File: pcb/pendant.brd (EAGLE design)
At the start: 24 x 99 mm, 45 parts, among them CON1 USB_MICROSMT+THRUHULE, Q2 16MHz, SW2 BUTTON_2, T1 SSM3J328R,LF, T2 SSM3J328R,LF, U2 MK20D--VFM5, U3 74LVC1G17DCK, U4 74LVC1G17DCK

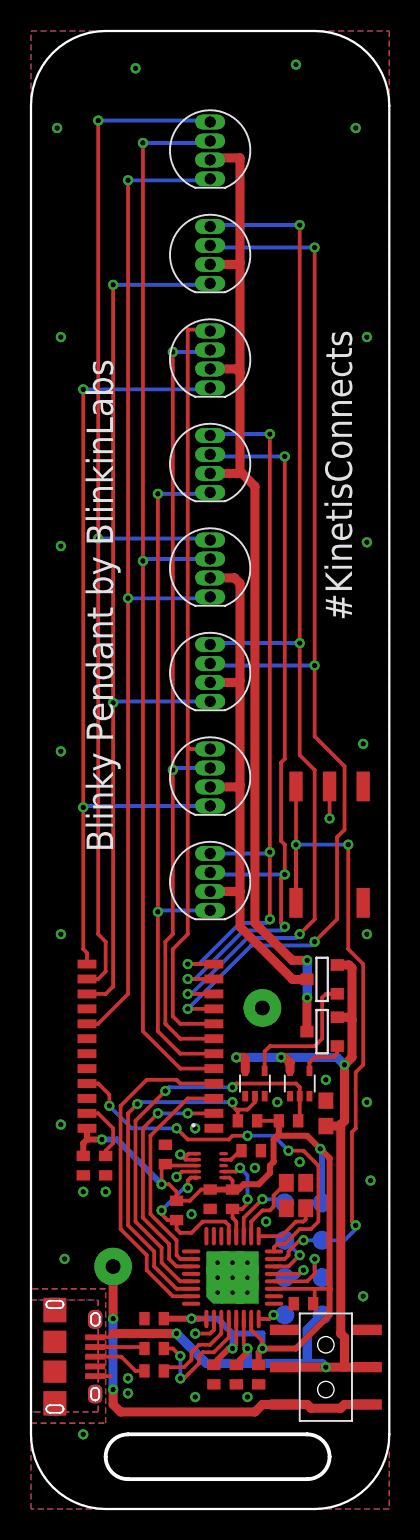
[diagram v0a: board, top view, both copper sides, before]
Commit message: fix cap under ICN2026, change led output order, use 5050 LEDs, replace power and tach switches, use 10 LEDs, move test points out from battery
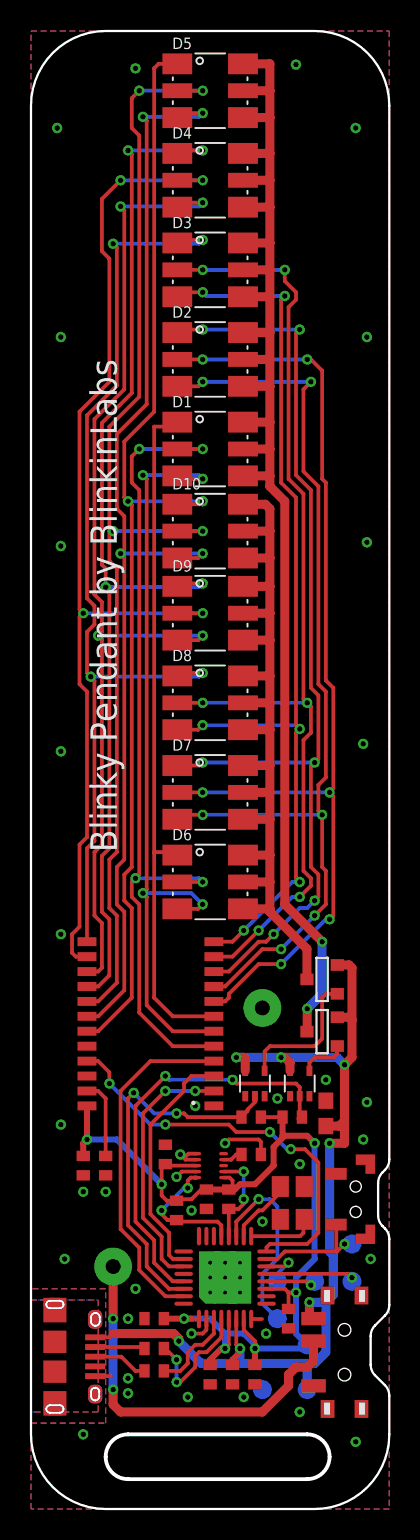
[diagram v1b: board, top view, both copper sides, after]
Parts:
- removed U$13: SWITCH_SPDTMSS-22C02, LeoBlinky2014:MSS-22C02
- added D10, D5: LED-RGB5050, blinkinlabs:LED-TRICOLOR-5050-FIXED
- added U$2: SWITCH_SPDT_SHIELD, blinkinlabs:SWITCH_SMD_90_DEGREE
- D1, D2, D3, D4, D6, D7, D8, D9: value LED-RGB-CA-THRUCLEAR -> LED-RGB5050; device SparkFun-LED:LED-RGB-THRU -> blinkinlabs:LED-TRICOLOR-5050-FIXED
- Q2: device blinkinlabs:CRSYTAL_2520 -> blinkinlabs:CRYSTAL_3225
- SW2: device blinkinlabs:TD-07XB -> blinkinlabs:BUTTON_MOMENTARY_MP5
- moved SW2 23.8 mm to (21.8, 20.8)
- moved TP2 9.55 mm to (18.5, 11.0)
- moved TP1 7.77 mm to (16.5, 12.8)
- moved TP5 5.22 mm to (15.5, 8.00)
- moved TP6 5.10 mm to (18.5, 8.00)
- moved TP7 4.51 mm to (21.5, 15.2)
- moved D9 3.00 mm to (12.0, 60.0), turned to 0 degrees
- moved TP4 2.80 mm to (16.5, 15.2)
- moved TP8 2.02 mm to (21.5, 17.8)
- moved D4 2.00 mm to (12.0, 89.0), turned to 0 degrees
- moved D8 2.00 mm to (12.0, 54.0), turned to 0 degrees
- moved U$5 1.50 mm to (8.00, 32.5)
- moved C15 1.41 mm to (17.2, 12.8), turned to 270 degrees
- moved D1 1.00 mm to (12.0, 71.0), turned to 0 degrees
- moved D3 1.00 mm to (12.0, 83.0), turned to 0 degrees
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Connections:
- removed net N$16: U$5.20
- net +5V: now also U$2.L1; no longer U$13.P0, U$13.P1
- net B0: now also D1.1, D6.1, U$5.7; no longer D1.4, D6.4, U$5.12
- net B1: now also D2.1, D7.1, U$5.10; no longer D2.4, D7.4, U$5.8
- net B2: now also D3.1, D8.1, U$5.13; no longer D3.4, D8.4, U$5.10
- net B3: now also D4.1, D9.1, U$5.16; no longer D4.4, D9.4, U$5.14
- net B4: now also D10.1, D5.1, U$5.19; no longer U$5.16
- net G0: now also U$5.6; no longer U$5.11
- net G1: now also U$5.9; no longer U$5.7
- net G2: now also U$5.12; no longer U$5.9
- net G3: now also U$5.15; no longer U$5.5
- net G4: now also D10.3, D5.3
- net GND: now also SW2.1, SW2.SHEILD_1, SW2.SHEILD_2, SW2.SHEILD_3, SW2.SHEILD_4, U$2.SHIELD_1, U$2.SHIELD_2, U$2.SHIELD_3, U$2.SHIELD_4; no longer SW2.3, SW2.4, SW2.5
- net N$2: now also U$2.COM; no longer U$13.O0, U$13.O1
- net R0: now also D1.2, D6.2, U$5.5; no longer D1.1, D6.1, U$5.6
- net R1: now also D2.2, D7.2, U$5.8; no longer D2.1, D7.1, U$5.13
- net R2: now also D3.2, D8.2, U$5.11; no longer D3.1, D8.1, U$5.15
- net R3: now also D4.2, D9.2, U$5.14; no longer D4.1, D9.1, U$5.17
- net R4: now also D10.2, D5.2, U$5.17; no longer U$5.19
- net S0: now also D1.4, D1.5, D1.6, D2.4, D2.5, D2.6, D3.4, D3.5, D3.6, D4.4, D4.5, D4.6, D5.4, D5.5, D5.6; no longer D1.2, D2.2, D3.2, D4.2
- net S1: now also D10.4, D10.5, D10.6, D6.4, D6.5, D6.6, D7.4, D7.5, D7.6, D8.4, D8.5, D8.6, D9.4, D9.5, D9.6; no longer D6.2, D7.2, D8.2, D9.2
- net TMS: no longer SW2.1
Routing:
- net R4: track 0.00 -> 78.0 mm, vias 0 -> 4
- net G4: track 0.00 -> 76.7 mm, vias 0 -> 4
- net B4: track 0.00 -> 76.1 mm, vias 0 -> 2
- net TMS: track 48.2 -> 7.81 mm, vias 4 -> 1
- net S0: track 69.4 -> 93.7 mm
- net S1: track 37.2 -> 59.7 mm
- net B1: track 52.5 -> 65.8 mm, vias 0 -> 6
- net R1: track 55.7 -> 67.8 mm, vias 2 -> 6
- net G2: track 74.4 -> 63.3 mm, vias 4 -> 6
- net G1: track 54.0 -> 64.9 mm, vias 2 -> 6
- net R0: track 47.5 -> 56.8 mm, vias 2 -> 4
- net RESET: track 4.60 -> 12.9 mm
- net B2: track 71.3 -> 65.8 mm
- net R2: track 62.0 -> 67.2 mm, vias 2 -> 6
- net +5V: track 70.8 -> 66.4 mm, vias 6 -> 7
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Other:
- outline, holes or cut-outs redrawn
- board text removed: "#KinetisConnects"
- board text removed: "+5"
- board text removed: "BLUE"
- board text removed: "GREEN"
- board text removed: "RED"

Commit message: Update battery footprint
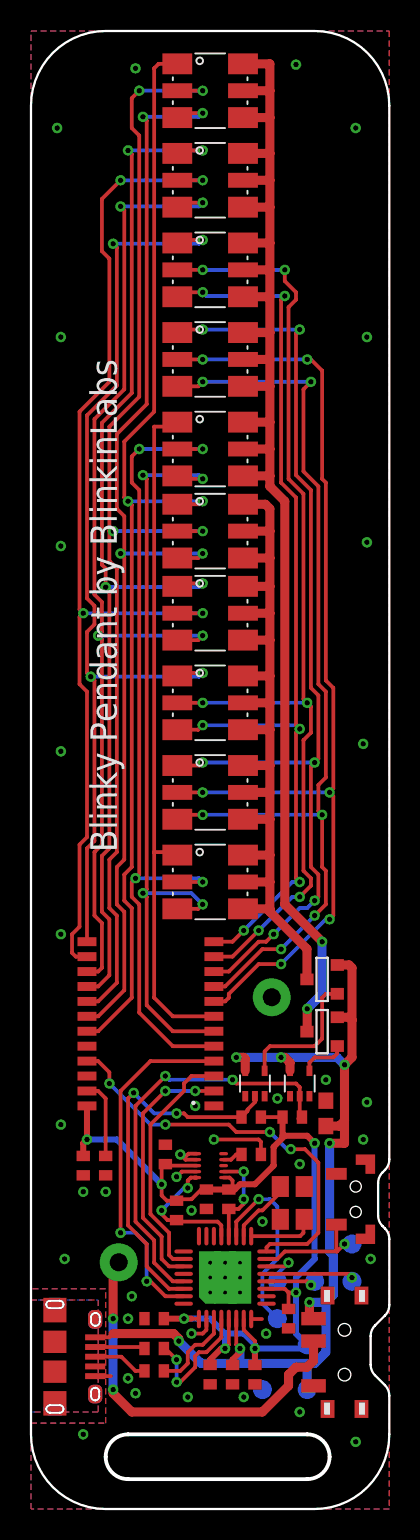
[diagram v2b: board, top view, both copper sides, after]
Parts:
- moved U$1 0.71 mm to (12.5, 28.0)
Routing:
- net LED_STROBE: track 23.3 -> 24.0 mm, vias 0 -> 2
- net GND: track 11.9 -> 12.6 mm
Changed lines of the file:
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@@
 <?xml version="1.0" encoding="utf-8"?>
 <!DOCTYPE eagle SYSTEM "eagle.dtd">
-<eagle version="7.1.0">
+<eagle version="7.2.0">
 <drawing>
 <settings>
@@
 <layer number="27" name="tValues" color="7" fill="1" visible="no" active="yes"/>
 <layer number="28" name="bValues" color="7" fill="1" visible="no" active="yes"/>
-<layer number="29" name="tStop" color="7" fill="3" visible="yes" active="yes"/>
+<layer number="29" name="tStop" color="7" fill="3" visible="no" active="yes"/>
 <layer number="30" name="bStop" color="7" fill="6" visible="no" active="yes"/>
-<layer number="31" name="tCream" color="13" fill="4" visible="yes" active="yes"/>
+<layer number="31" name="tCream" color="13" fill="4" visible="no" active="yes"/>
 <layer number="32" name="bCream" color="7" fill="5" visible="no" active="yes"/>
 <layer number="33" name="tFinish" color="6" fill="3" visible="no" active="yes"/>
 <layer number="34" name="bFinish" color="6" fill="6" visible="no" active="yes"/>
 <layer number="35" name="tGlue" color="7" fill="4" visible="no" active="yes"/>
-<layer number="36" name="bGlue" color="7" fill="5" visible="yes" active="yes"/>
+<layer number="36" name="bGlue" color="7" fill="5" visible="no" active="yes"/>
 <layer number="37" name="tTest" color="7" fill="1" visible="no" active="yes"/>
 <layer number="38" name="bTest" color="7" fill="1" visible="no" active="yes"/>
@@
 <element name="C3" library="adafruit" package="C0402" value="100nF" x="11.75" y="20.75" smashed="yes" rot="R270"/>
 <element name="C5" library="adafruit" package="C0402" value="100nF" x="9" y="23.75" smashed="yes" rot="R90"/>
-<element name="D1" library="blinkinlabs" package="LED-TRICOLOR-5050-FIXED" value="LED-RGB5050" x="12" y="71"/>
-<element name="D2" library="blinkinlabs" package="LED-TRICOLOR-5050-FIXED" value="LED-RGB5050" x="12" y="77"/>
-<element name="D3" library="blinkinlabs" package="LED-TRICOLOR-5050-FIXED" value="LED-RGB5050" x="12" y="83"/>
-<element name="D4" library="blinkinlabs" package="LED-TRICOLOR-5050-FIXED" value="LED-RGB5050" x="12" y="89"/>
-<element name="D6" library="blinkinlabs" package="LED-TRICOLOR-5050-FIXED" value="LED-RGB5050" x="12" y="42"/>
-<element name="D7" library="blinkinlabs" package="LED-TRICOLOR-5050-FIXED" value="LED-RGB5050" x="12" y="48"/>
-<element name="D8" library="blinkinlabs" package="LED-TRICOLOR-5050-FIXED" value="LED-RGB5050" x="12" y="54"/>
-<element name="D9" library="blinkinlabs" package="LED-TRICOLOR-5050-FIXED" value="LED-RGB5050" x="12" y="60"/>
+<element name="D1" library="blinkinlabs" package="LED-TRICOLOR-5050-FIXED" value="LED-RGB5050" x="12" y="71" smashed="yes">
+<attribute name="VALUE" x="9.46" y="67.444" size="0.762" layer="27"/>
+</element>
+<element name="D2" library="blinkinlabs" package="LED-TRICOLOR-5050-FIXED" value="LED-RGB5050" x="12" y="77" smashed="yes">
+<attribute name="VALUE" x="9.46" y="73.444" size="0.762" layer="27"/>
+</element>
+<element name="D3" library="blinkinlabs" package="LED-TRICOLOR-5050-FIXED" value="LED-RGB5050" x="12" y="83" smashed="yes">
+<attribute name="VALUE" x="9.46" y="79.444" size="0.762" layer="27"/>
+</element>
+<element name="D4" library="blinkinlabs" package="LED-TRICOLOR-5050-FIXED" value="LED-RGB5050" x="12" y="89" smashed="yes">
+<attribute name="VALUE" x="9.46" y="85.444" size="0.762" layer="27"/>
+</element>
+<element name="D6" library="blinkinlabs" package="LED-TRICOLOR-5050-FIXED" value="LED-RGB5050" x="12" y="42" smashed="yes">
+<attribute name="VALUE" x="9.46" y="38.444" size="0.762" layer="27"/>
+</element>
+<element name="D7" library="blinkinlabs" package="LED-TRICOLOR-5050-FIXED" value="LED-RGB5050" x="12" y="48" smashed="yes">
+<attribute name="VALUE" x="9.46" y="44.444" size="0.762" layer="27"/>
+</element>
+<element name="D8" library="blinkinlabs" package="LED-TRICOLOR-5050-FIXED" value="LED-RGB5050" x="12" y="54" smashed="yes">
+<attribute name="VALUE" x="9.46" y="50.444" size="0.762" layer="27"/>
+</element>
+<element name="D9" library="blinkinlabs" package="LED-TRICOLOR-5050-FIXED" value="LED-RGB5050" x="12" y="60" smashed="yes">
+<attribute name="VALUE" x="9.46" y="56.444" size="0.762" layer="27"/>
+</element>
 <element name="C11" library="adafruit" package="C0402" value="100nF" x="15" y="9" smashed="yes" rot="R270">
 <attribute name="VALUE" x="13.095" y="9.635" size="1.27" layer="27" rot="R270"/>
@@
 <attribute name="TP_SIGNAL_NAME" value="" x="16.5" y="12.75" size="1.778" layer="28" rot="MR0" display="off"/>
 </element>
-<element name="U$1" library="blinkinlabs" package="CR2032X2" value="CR2032X2" x="12" y="27.5" rot="MR300"/>
+<element name="U$1" library="blinkinlabs" package="CR2032X2" value="CR2032X2" x="12.5" y="28" rot="MR300"/>
 <element name="T1" library="zetex" package="SOT-23" value="SSM3J328R,LF" x="19.5" y="32" smashed="yes" rot="R270">
 <attribute name="OC_NEWARK" value="unknown" x="19.5" y="32" size="1.778" layer="27" rot="R270" display="off"/>
@@
 <attribute name="VALUE" x="16.575" y="23.585" size="1.27" layer="27" rot="R270"/>
 </element>
-<element name="D5" library="blinkinlabs" package="LED-TRICOLOR-5050-FIXED" value="LED-RGB5050" x="12" y="95"/>
-<element name="D10" library="blinkinlabs" package="LED-TRICOLOR-5050-FIXED" value="LED-RGB5050" x="12" y="65.5"/>
+<element name="D5" library="blinkinlabs" package="LED-TRICOLOR-5050-FIXED" value="LED-RGB5050" x="12" y="95" smashed="yes">
+<attribute name="VALUE" x="9.46" y="91.444" size="0.762" layer="27"/>
+</element>
+<element name="D10" library="blinkinlabs" package="LED-TRICOLOR-5050-FIXED" value="LED-RGB5050" x="12" y="65.5" smashed="yes">
+<attribute name="VALUE" x="9.46" y="61.944" size="0.762" layer="27"/>
+</element>
 <element name="U$2" library="blinkinlabs" package="SWITCH_SMD_90_DEGREE" value="SWITCH_SPDT_SHIELD" x="21" y="10.5" smashed="yes" rot="R270">
 <attribute name="VALUE" x="24" y="9.5" size="0.762" layer="27" rot="R270"/>
@@
 <via x="19.75" y="28.75" extent="1-16" drill="0.35"/>
 <via x="11" y="27" extent="1-16" drill="0.35"/>
-<via x="13" y="24.5" extent="1-16" drill="0.35"/>
+<via x="12.25" y="24.75" extent="1-16" drill="0.35"/>
 <wire x1="11.1" y1="22.6" x2="10.1" y2="22.6" width="0.254" layer="1"/>
 <wire x1="10.1" y1="22.6" x2="9.75" y2="22.25" width="0.254" layer="1"/>
@@
 <via x="22.5" y="27.25" extent="1-16" drill="0.35"/>
 <contactref element="U$1" pad="-"/>
-<via x="6.5" y="7.75" extent="1-16" drill="0.35"/>
+<via x="7" y="7.75" extent="1-16" drill="0.35"/>
 <via x="2.25" y="16.75" extent="1-16" drill="0.35"/>
 <via x="2" y="25.75" extent="1-16" drill="0.35"/>
@@
 <via x="18" y="6.5" extent="1-16" drill="0.35"/>
 <via x="21.75" y="4.5" extent="1-16" drill="0.35"/>
-<via x="7" y="14.75" extent="1-16" drill="0.35"/>
+<via x="6.75" y="14.25" extent="1-16" drill="0.35"/>
 <contactref element="SW2" pad="SHEILD_2"/>
 <contactref element="SW2" pad="SHEILD_3"/>
@@
 <wire x1="15.4" y1="23.75" x2="15.4" y2="24.6" width="0.254" layer="1"/>
 <wire x1="15.4" y1="24.6" x2="15.25" y2="24.75" width="0.254" layer="1"/>
-<wire x1="15.25" y1="24.75" x2="13.25" y2="24.75" width="0.254" layer="1"/>
-<wire x1="13.25" y1="24.75" x2="13" y2="24.5" width="0.254" layer="1"/>
+<wire x1="15.25" y1="24.75" x2="12.25" y2="24.75" width="0.254" layer="1"/>
 </signal>
 <signal name="LED_OE">
@@
 <wire x1="12.25" y1="30" x2="8" y2="30" width="0.254" layer="1"/>
 <wire x1="8" y1="30" x2="6" y2="28" width="0.254" layer="1"/>
-<wire x1="6" y1="28" x2="6" y2="18.75" width="0.254" layer="1"/>
+<wire x1="6" y1="28" x2="6" y2="18.5" width="0.254" layer="1"/>
 <wire x1="10.225" y1="14.25" x2="9" y2="14.25" width="0.254" layer="1"/>
-<wire x1="9" y1="14.25" x2="7.25" y2="16" width="0.254" layer="1"/>
-<wire x1="7.25" y1="16" x2="7.25" y2="17.5" width="0.254" layer="1"/>
-<wire x1="7.25" y1="17.5" x2="6" y2="18.75" width="0.254" layer="1"/>
+<via x="6" y="18.5" extent="1-16" drill="0.35"/>
+<wire x1="6" y1="18.5" x2="7" y2="18.5" width="0.254" layer="16"/>
+<wire x1="7" y1="18.5" x2="7.75" y2="17.75" width="0.254" layer="16"/>
+<wire x1="7.75" y1="17.75" x2="7.75" y2="15.25" width="0.254" layer="16"/>
+<via x="7.75" y="15.25" extent="1-16" drill="0.35"/>
+<wire x1="7.75" y1="15.25" x2="8" y2="15.25" width="0.254" layer="1"/>
+<wire x1="8" y1="15.25" x2="9" y2="14.25" width="0.254" layer="1"/>
 </signal>
 <signal name="LED_S0">
@@
 <signal name="N$2">
 <contactref element="U$1" pad="+"/>
-<wire x1="5.5" y1="16.24166875" x2="5.5" y2="12.75" width="0.6096" layer="1"/>
+<wire x1="5.875" y1="16.5251625" x2="5.5" y2="16.1501625" width="0.6096" layer="1"/>
+<wire x1="5.5" y1="16.1501625" x2="5.5" y2="12.75" width="0.6096" layer="1"/>
 <via x="5.5" y="12.75" extent="1-16" drill="0.35"/>
 <wire x1="5.5" y1="12.75" x2="5.5" y2="8" width="0.6096" layer="16"/>
 <via x="5.5" y="8" extent="1-16" drill="0.35"/>
-<wire x1="5.5" y1="8" x2="5.5" y2="7" width="0.6096" layer="1"/>
-<wire x1="5.5" y1="7" x2="6" y2="6.5" width="0.6096" layer="1"/>
-<wire x1="6" y1="6.5" x2="15.5" y2="6.5" width="0.6096" layer="1"/>
+<wire x1="5.5" y1="8" x2="5.5" y2="7.75" width="0.6096" layer="1"/>
+<wire x1="5.5" y1="7.75" x2="6.75" y2="6.5" width="0.6096" layer="1"/>
+<wire x1="6.75" y1="6.5" x2="15.5" y2="6.5" width="0.6096" layer="1"/>
 <wire x1="15.5" y1="6.5" x2="17.25" y2="8.25" width="0.6096" layer="1"/>
 <contactref element="U$2" pad="COM"/>
